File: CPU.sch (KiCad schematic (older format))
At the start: 6 parts

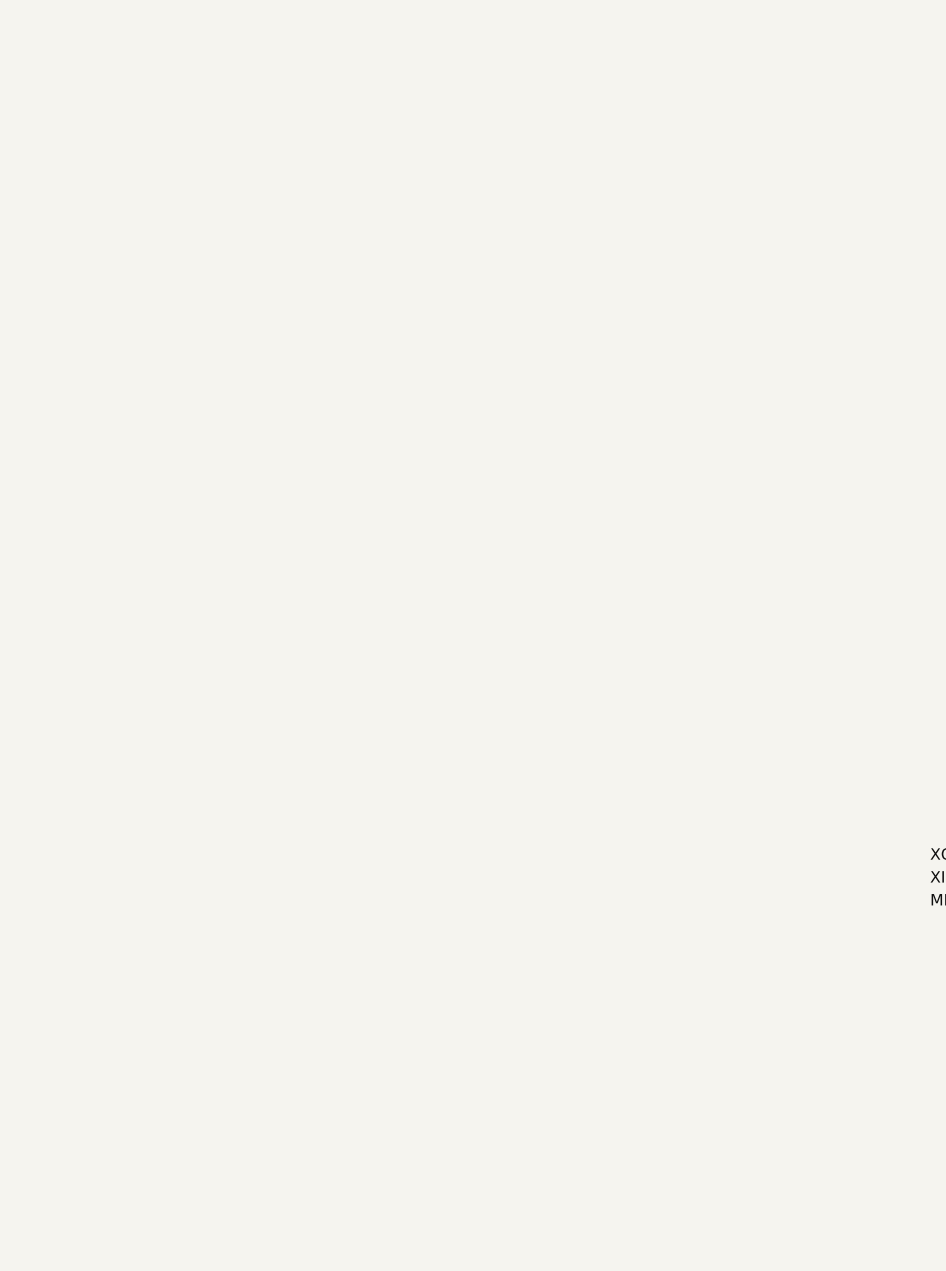
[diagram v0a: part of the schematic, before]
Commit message: added CPU to CPU sheeT
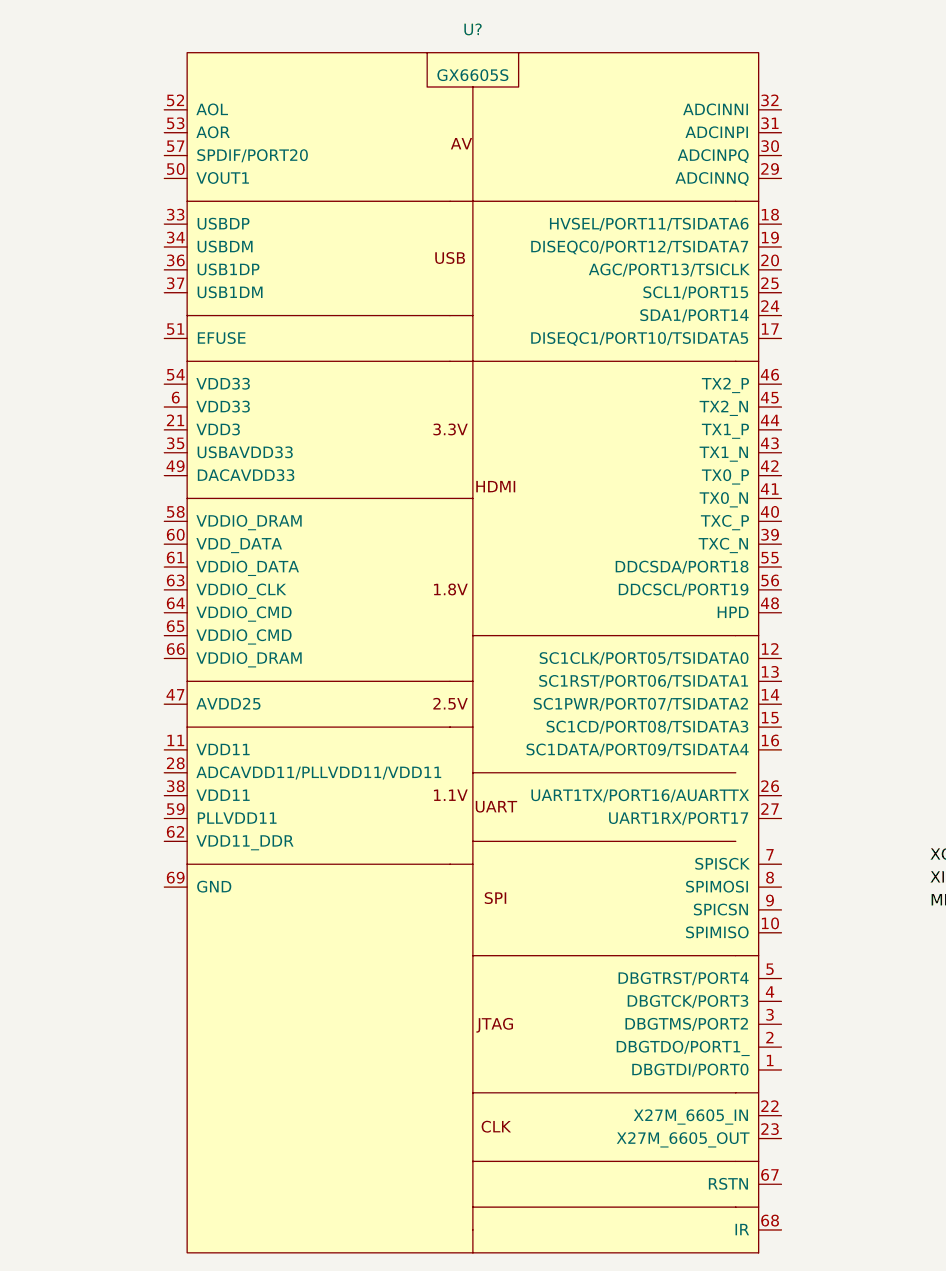
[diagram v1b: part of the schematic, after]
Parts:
- added U?: GX6605S, symbol csky:GX6605S
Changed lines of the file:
@@
 Wire Wire Line
 	2200 5000 2400 5000
+$Comp
+L csky:GX6605S U?
+U 1 1 5F4A8034
+P 5950 1000
+F 0 "U?" H 5950 1300 50  0000 C CNN
+F 1 "GX6605S" H 5950 1100 50  0000 C CNN
+F 2 "" H 5850 1150 50  0001 C CNN
+F 3 "" H 5850 1150 50  0001 C CNN
+	1    5950 1000
+	1    0    0    -1
+$EndComp
 $EndSCHEMATC

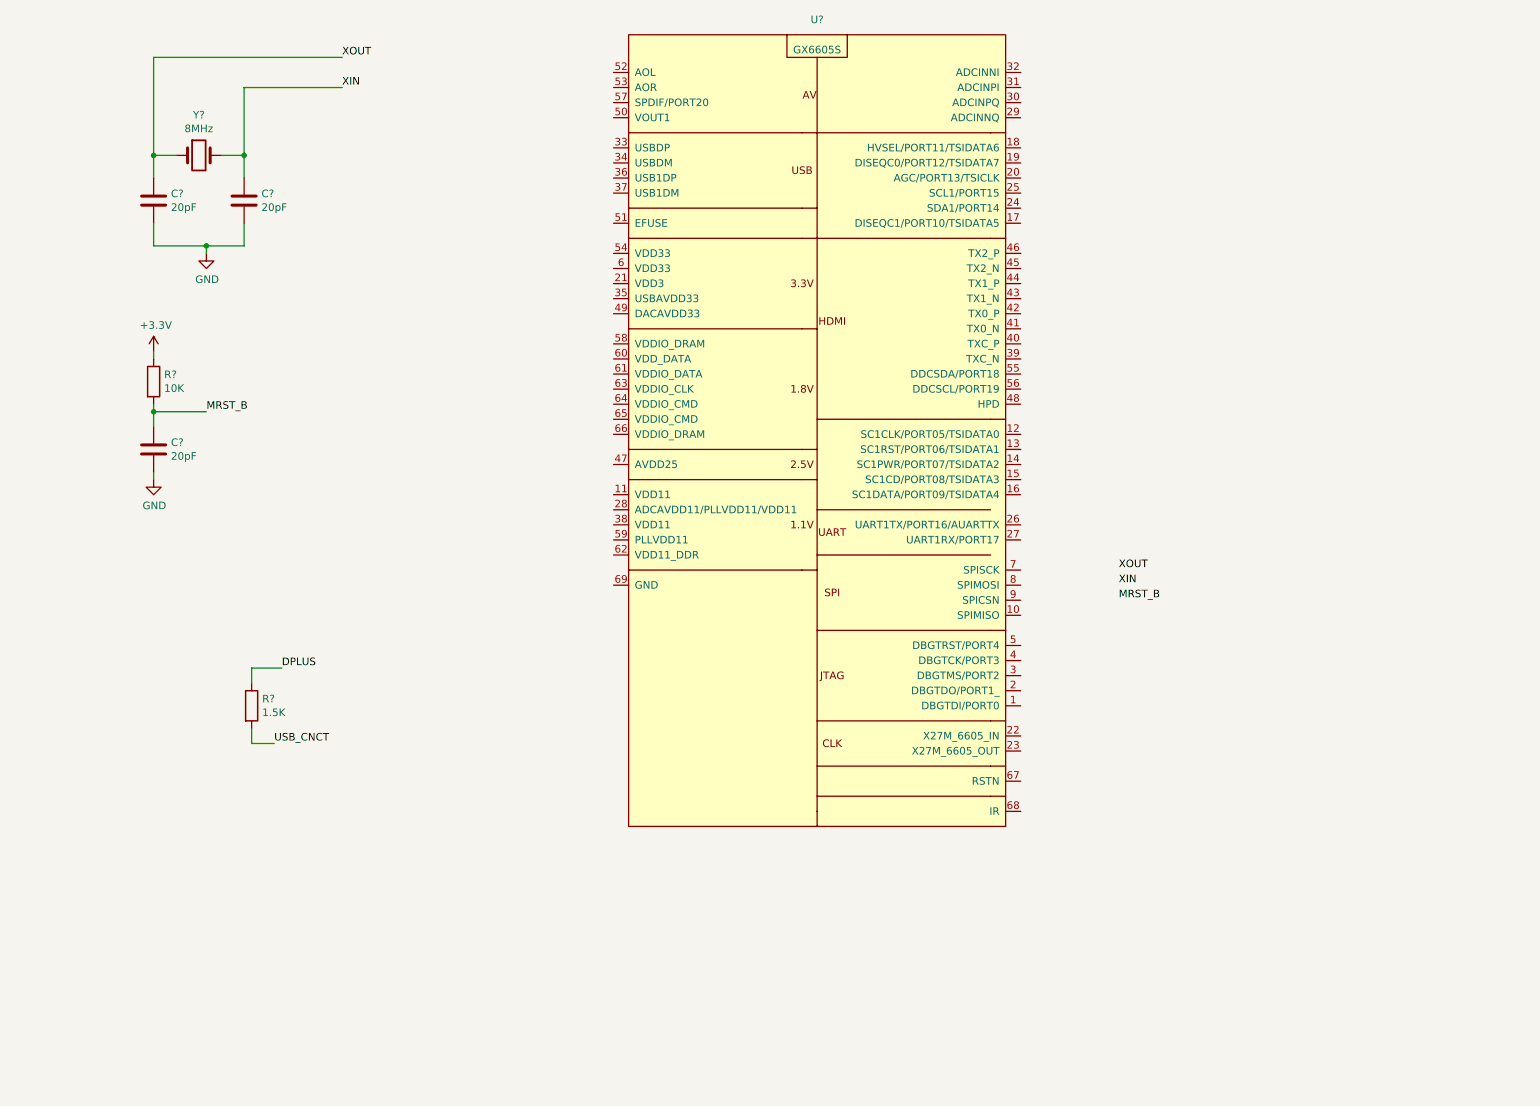
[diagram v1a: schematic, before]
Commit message: added power to CPU
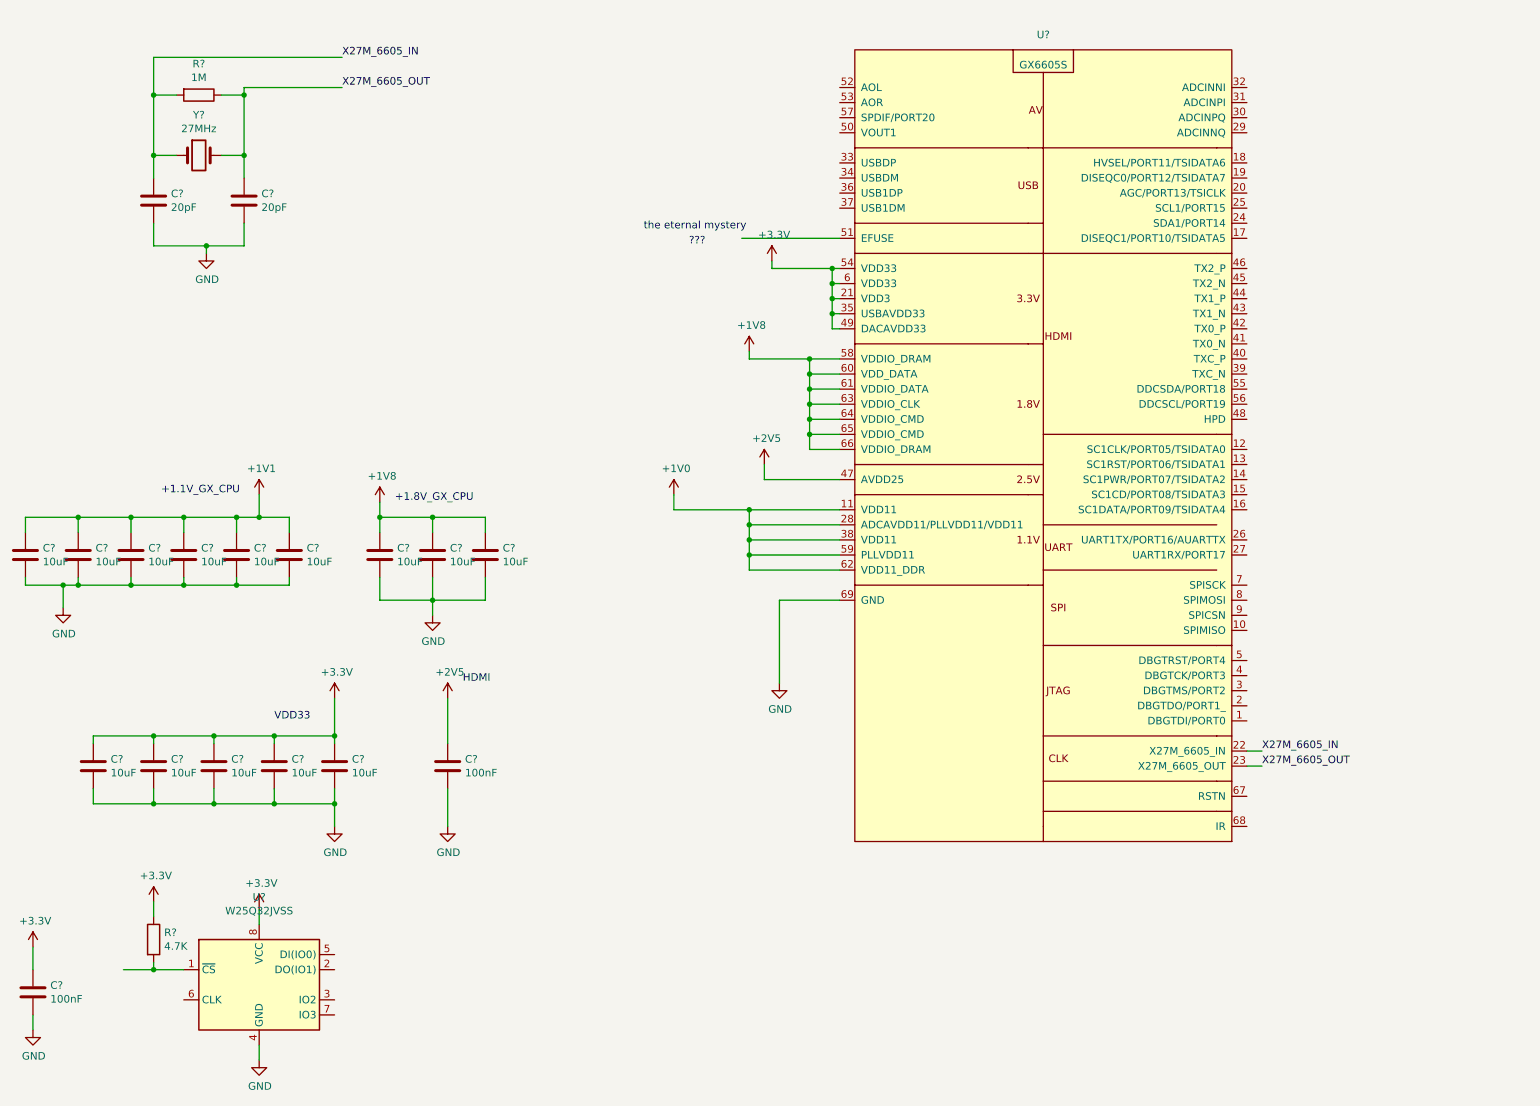
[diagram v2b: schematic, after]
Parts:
- removed C?: 20pF, symbol Device:C
- removed R?: 10K, symbol Device:R
- removed R?: 1.5K, symbol Device:R
- added C? (x14): 10uF, symbol Device:C
- added C? (x2): 100nF, symbol Device:C
- added R?: 1M, symbol Device:R
- added R?: 4.7K, symbol Device:R
- added U?: W25Q32JVSS, Package_SO:SOIC-8_5.23x5.23mm_P1.27mm, symbol Memory_Flash:W25Q32JVSS
- Y?: value 8MHz -> 27MHz
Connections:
- net XIN is gone; now on net X27M_6605_OUT: C?.1, Y?.2
- net XOUT is gone; now on net X27M_6605_IN: C?.1, Y?.1
- net +3V3: now also U?.21 (VDD3), U?.35 (USBAVDD33), U?.49 (DACAVDD33), U?.54 (VDD33), U?.6 (VDD33), C?.1, C?.1, C?.1, C?.1, C?.1, C?.1, R?.1, U?.8 (VCC)
- net GND: now also U?.69 (GND), C?.2, C?.2, C?.2, C?.2, C?.2, C?.2, C?.2, C?.2, C?.2, C?.2, C?.2, C?.2, C?.2, C?.2, C?.2, C?.2, U?.4 (GND)
- net +1V0: now reaches U?.11 (VDD11)
- net +1V0: now also U?.28 (ADCAVDD11/PLLVDD11/VDD11), U?.38 (VDD11), U?.59 (PLLVDD11), U?.62 (VDD11_DDR)
- net X27M_6605_IN: now reaches U?.22 (X27M_6605_IN)
- net X27M_6605_IN: now also R?.2
- net X27M_6605_OUT: now reaches U?.23 (X27M_6605_OUT)
- net X27M_6605_OUT: now also R?.1
- net +2V5: now reaches U?.47 (AVDD25)
- net +2V5: now also C?.1
- net +1V8: now reaches U?.58 (VDDIO_DRAM)
- net +1V8: now also U?.60 (VDD_DATA), U?.61 (VDDIO_DATA), U?.63 (VDDIO_CLK), U?.64 (VDDIO_CMD), U?.65 (VDDIO_CMD), U?.66 (VDDIO_DRAM), C?.1, C?.1, C?.1
- new net: R?.2, U?.1 (~CS)
- new net +1V1: C?.1, C?.1, C?.1, C?.1, C?.1, C?.1
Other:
- note added: "+1.1V_GX_CPU"
- note added: "+1.8V_GX_CPU\n"
- note added: "???\n"
- note added: "HDMI"
- note added: "VDD33\n"
- note added: "the eternal mystery"
- moved on the sheet: U?

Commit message: wired SPI flash to cpu, and added CPU lables
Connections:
- net +3V3: now also U?.3 (IO2), U?.7 (IO3)
- net SPI_MISO: now reaches U?.10 (SPIMISO)
- net SPI_MISO: now also U?.2 (DO(IO1))
- net TXC_N: now reaches U?.39 (TXC_N)
- net TXC_P: now reaches U?.40 (TXC_P)
- net TX0_N: now reaches U?.41 (TX0_N)
- net TX0_P: now reaches U?.42 (TX0_P)
- net TX1_N: now reaches U?.43 (TX1_N)
- net TX1_P: now reaches U?.44 (TX1_P)
- net TX2_N: now reaches U?.45 (TX2_N)
- net TX2_P: now reaches U?.46 (TX2_P)
- net HDMI_PLG: now reaches U?.48 (HPD)
- net HDMI_SDA: now reaches U?.55 (DDCSDA/PORT18)
- net HDMI_SCL: now reaches U?.56 (DDCSCL/PORT19)
- net NRST_GX_CPU: now reaches U?.67 (RSTN)
- net SPI_CLK: now reaches U?.7 (SPISCK)
- net SPI_CLK: now also U?.6 (CLK)
- net SPI_MOSI: now reaches U?.8 (SPIMOSI)
- net SPI_MOSI: now also U?.5 (DI(IO0))
- net SPI_CSN: now reaches U?.9 (SPICSN)
- net SPI_CSN: now also R?.2, U?.1 (~CS)
- no-connect marks 0 -> 5
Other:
- note added: "Main Serial port. tty0"
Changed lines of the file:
@@
 	1    0    0    -1
 $EndComp
+NoConn ~ 8800 1150
+NoConn ~ 8800 1250
+NoConn ~ 8800 1350
+NoConn ~ 8800 1450
+NoConn ~ 8800 6050
+Text GLabel 8900 5850 2    50   Output ~ 0
+NRST_GX_CPU
+Wire Wire Line
+	8900 5850 8800 5850
+Text Label 2950 7000 0    50   ~ 0
+SPI_MISO
+Wire Wire Line
+	2950 7000 2750 7000
+Text Label 9050 4750 0    50   ~ 0
+SPI_MISO
+Wire Wire Line
+	8800 4750 9050 4750
+Text Label 9050 4650 0    50   ~ 0
+SPI_CSN
+Wire Wire Line
+	9050 4650 8800 4650
+Text Label 1350 7000 2    50   ~ 0
+SPI_CSN
+Text Label 2950 6900 0    50   ~ 0
+SPI_MOSI
+Wire Wire Line
+	2950 6900 2750 6900
+Text Label 9050 4550 0    50   ~ 0
+SPI_MOSI
+Wire Wire Line
+	8800 4550 9050 4550
+Text Label 9050 4450 0    50   ~ 0
+SPI_CLK
+Text Label 1550 7200 2    50   ~ 0
+SPI_CLK
+Wire Wire Line
+	1550 7200 1750 7200
+Wire Wire Line
+	9050 4450 8800 4450
+$Comp
+L power:+3.3V #PWR?
+U 1 1 5F54869D
+P 3500 6950
+F 0 "#PWR?" H 3500 6800 50  0001 C CNN
+F 1 "+3.3V" H 3515 7123 50  0000 C CNN
+F 2 "" H 3500 6950 50  0001 C CNN
+F 3 "" H 3500 6950 50  0001 C CNN
+	1    3500 6950
+	1    0    0    -1
+$EndComp
+Wire Wire Line
+	2750 7300 3500 7300
+Wire Wire Line
+	3500 7300 3500 7200
+Wire Wire Line
+	2750 7200 3500 7200
+Connection ~ 3500 7200
+Wire Wire Line
+	3500 7200 3500 6950
+Text Notes 9250 4200 0    50   ~ 0
+Main Serial port. tty0
+Wire Wire Line
+	8800 4150 9050 4150
+Wire Wire Line
+	8800 4250 9050 4250
+Text GLabel 8900 3350 2    50   Input ~ 0
+HDMI_PLG
+Text GLabel 8900 3250 2    50   BiDi ~ 0
+HDMI_SCL
+Text GLabel 8900 3150 2    50   BiDi ~ 0
+HDMI_SDA
+Text GLabel 9500 3050 2    50   Output ~ 0
+TXC_N
+Text GLabel 9500 2950 2    50   Output ~ 0
+TXC_P
+Text GLabel 9500 2850 2    50   Output ~ 0
+TX0_N
+Text GLabel 9500 2750 2    50   Output ~ 0
+TX0_P
+Text GLabel 9500 2550 2    50   Output ~ 0
+TX1_P
+Text GLabel 9500 2650 2    50   Output ~ 0
+TX1_N
+Text GLabel 9500 2350 2    50   Output ~ 0
+TX2_P
+Text GLabel 9500 2450 2    50   Output ~ 0
+TX2_N
+Wire Wire Line
+	9500 2350 8800 2350
+Wire Wire Line
+	8800 2450 9500 2450
+Wire Wire Line
+	9500 2550 8800 2550
+Wire Wire Line
+	8800 2650 9500 2650
+Wire Wire Line
+	9500 2750 8800 2750
+Wire Wire Line
+	8800 2850 9500 2850
+Wire Wire Line
+	9500 2950 8800 2950
+Wire Wire Line
+	8800 3050 9500 3050
+Wire Wire Line
+	8900 3150 8800 3150
+Wire Wire Line
+	8800 3250 8900 3250
+Wire Wire Line
+	8900 3350 8800 3350
 $EndSCHEMATC

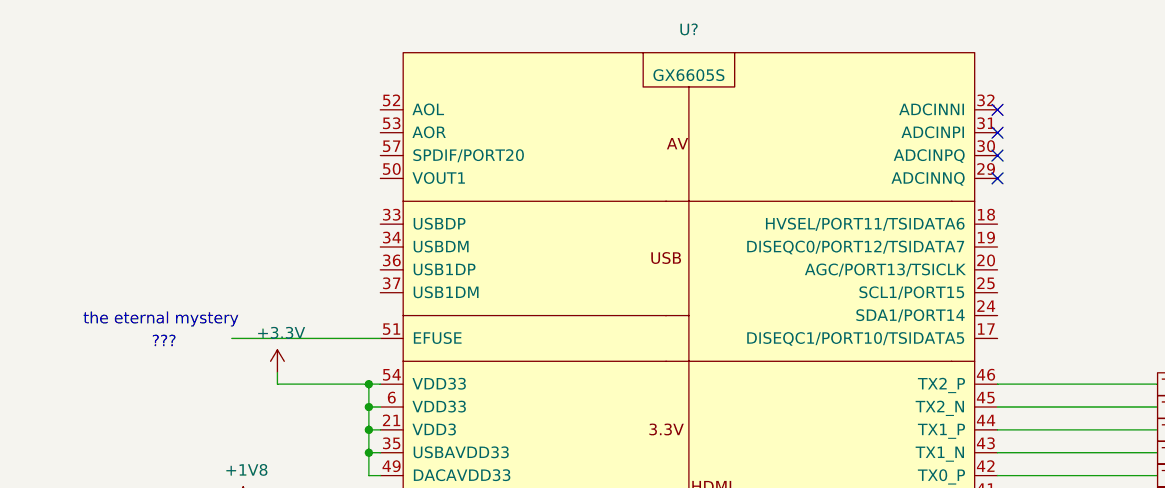
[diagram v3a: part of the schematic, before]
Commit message: added port / GPIO sheet to scimatic
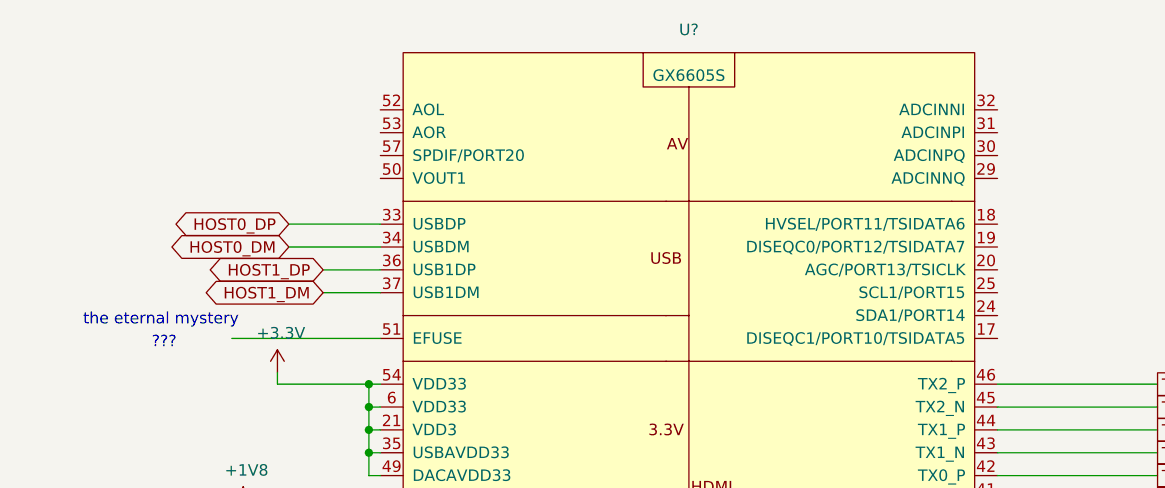
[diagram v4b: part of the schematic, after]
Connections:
- net HOST0_DP: now reaches U?.33 (USBDP)
- net HOST0_DM: now reaches U?.34 (USBDM)
- net HOST1_DP: now reaches U?.36 (USB1DP)
- net HOST1_DM: now reaches U?.37 (USB1DM)
- no-connect marks 5 -> 1
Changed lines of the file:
@@
 $Descr A4 11693 8268
 encoding utf-8
-Sheet 3 3
+Sheet 3 4
 Title ""
 Date ""
@@
 	1    0    0    -1
 $EndComp
-NoConn ~ 8800 1150
-NoConn ~ 8800 1250
-NoConn ~ 8800 1350
-NoConn ~ 8800 1450
 NoConn ~ 8800 6050
 Text GLabel 8900 5850 2    50   Output ~ 0
@@
 Wire Wire Line
 	8900 3350 8800 3350
+Text GLabel 5850 1950 0    50   BiDi ~ 0
+HOST1_DM
+Text GLabel 5850 1850 0    50   BiDi ~ 0
+HOST1_DP
+Text GLabel 5700 1750 0    50   BiDi ~ 0
+HOST0_DM
+Text GLabel 5700 1650 0    50   BiDi ~ 0
+HOST0_DP
+Wire Wire Line
+	5700 1650 6100 1650
+Wire Wire Line
+	5700 1750 6100 1750
+Wire Wire Line
+	5850 1850 6100 1850
+Wire Wire Line
+	6100 1950 5850 1950
 $EndSCHEMATC
